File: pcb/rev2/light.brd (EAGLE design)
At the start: 13 x 13 mm, 5 parts, among them J3 FFC3B07-05-T, U1 TEMT6000

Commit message: working on improvments
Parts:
- removed JP1: (no value), adafruit_changed:1X03-CLEANBIG
- added U$1: LS_VERT, apricot:LS_VERT
- moved C1 6.87 mm to (2.79, 5.84), turned to 0 degrees
- moved J3 6.37 mm to (7.85, 11.6), turned to 180 degrees
- moved U1 4.33 mm to (7.85, 4.34), turned to 180 degrees
- moved R5 4.16 mm to (13.1, 5.84), turned to 180 degrees
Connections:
- net +3V3: now also U$1.B1, U$1.B2; no longer JP1.1
- net GND: now also U$1.T1, U$1.T2; no longer JP1.2
- net S: now also U$1.B3, U$1.B4, U$1.T3, U$1.T4; no longer JP1.3
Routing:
- net GND: track 0.00 -> 6.50 mm
- net S: track 9.12 -> 13.7 mm, vias 0 -> 1
- net +3V3: track 17.1 -> 21.2 mm, vias 0 -> 1
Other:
- board size 13 x 13 mm -> 15.7 x 15.6 mm
- board text added: "PulseHPT.com"
- board text removed: "G"
- board text removed: "PulseHPT.com dekuNukem 2023"
- board text removed: "S"
- board text removed: "V"

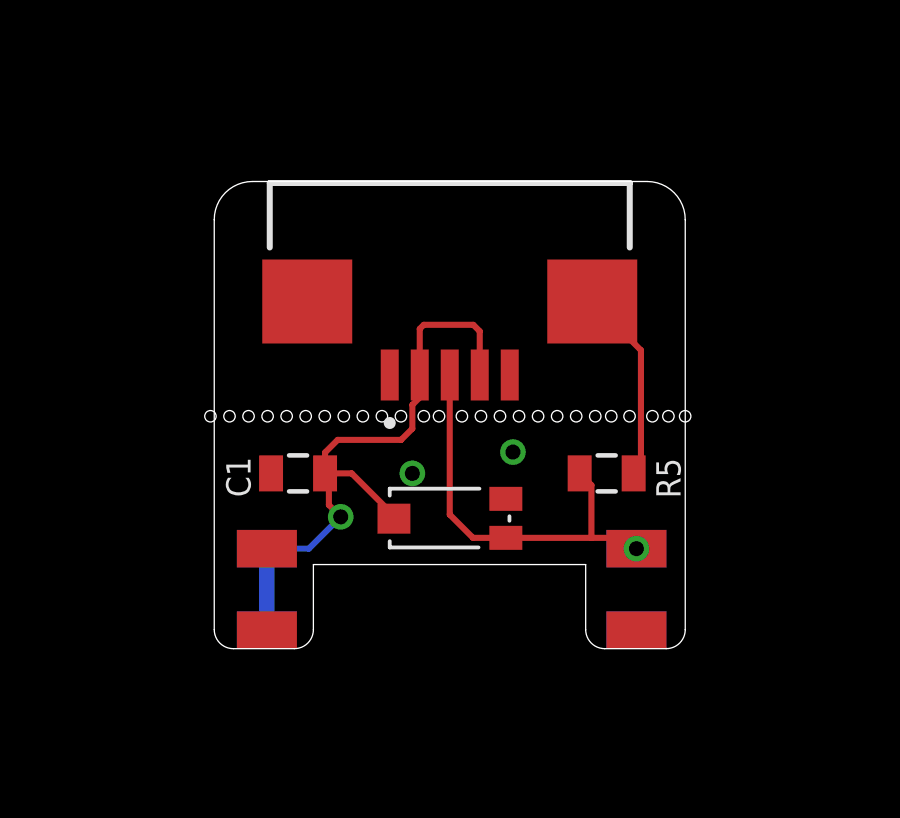
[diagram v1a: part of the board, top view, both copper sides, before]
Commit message: adjusted for pcb thickness
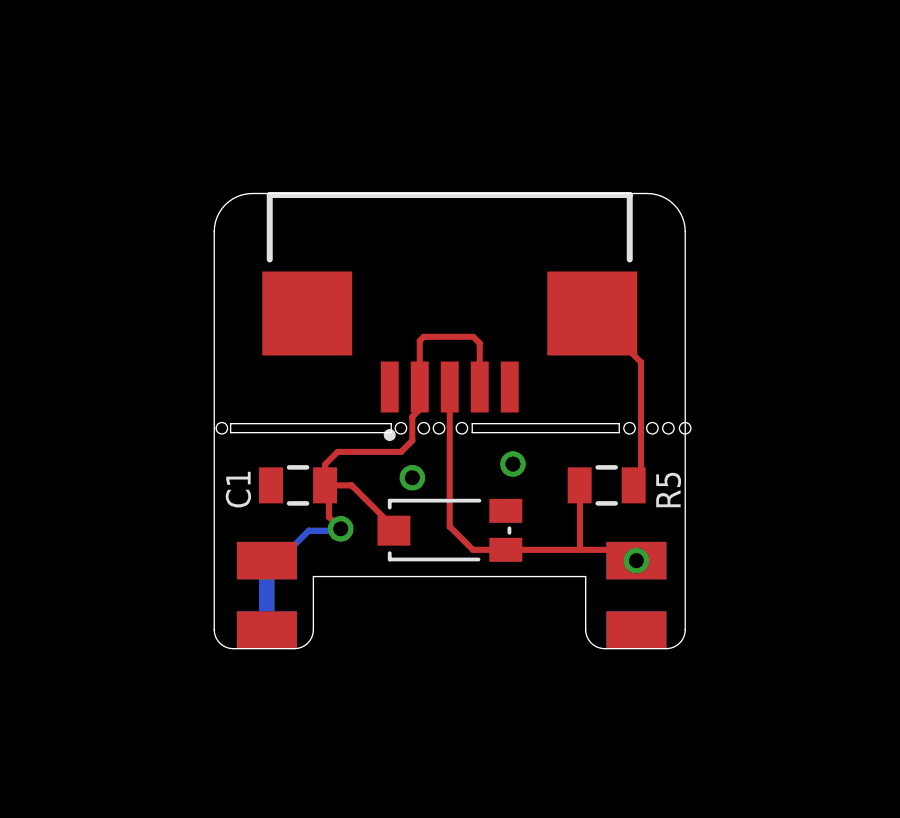
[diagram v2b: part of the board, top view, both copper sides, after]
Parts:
- moved U1 0.40 mm to (7.85, 3.94)
- moved C1 0.40 mm to (2.79, 5.44)
- moved R5 0.40 mm to (13.1, 5.44)
- moved J3 0.40 mm to (7.85, 11.2)
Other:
- board size 15.7 x 15.6 mm -> 15.7 x 15.2 mm

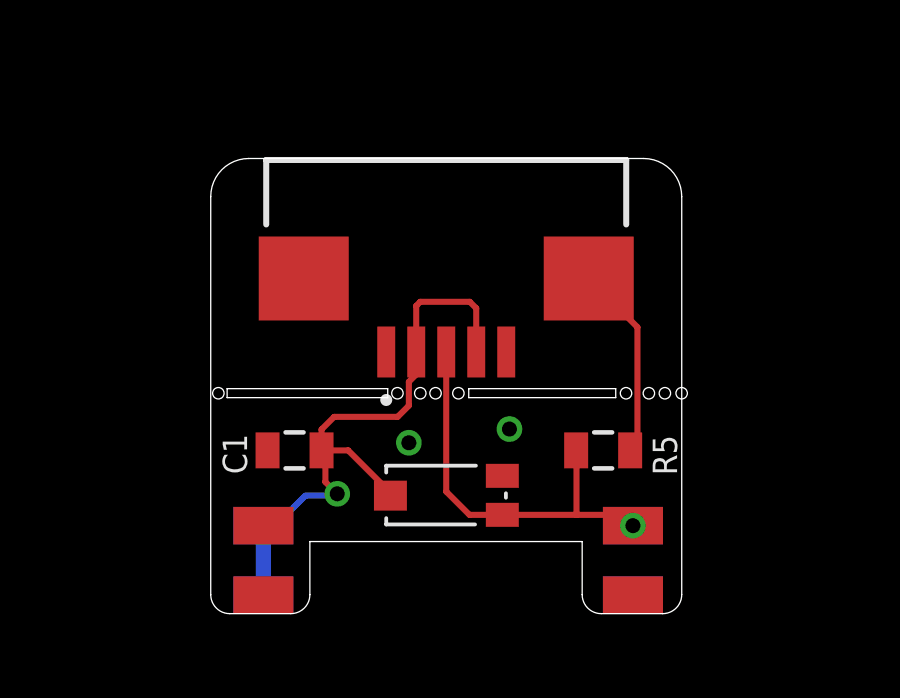
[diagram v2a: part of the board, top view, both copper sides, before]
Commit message: adjusted for pcb thickness
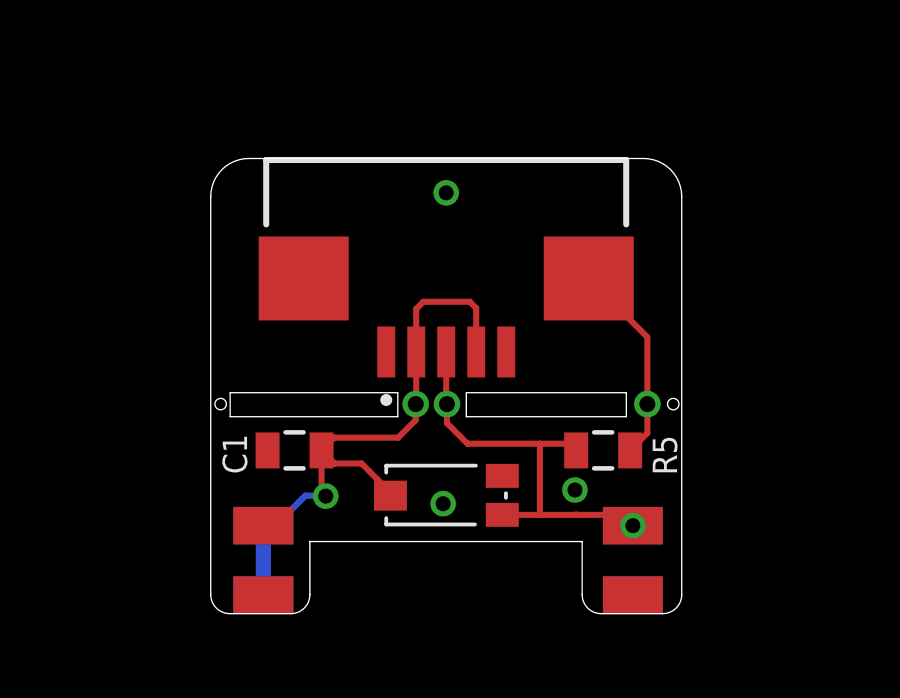
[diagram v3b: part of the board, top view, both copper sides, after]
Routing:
- net +3V3: track 20.8 -> 20.3 mm, vias 1 -> 2
- net S: track 13.7 -> 14.2 mm, vias 1 -> 2
- net GND: track 6.50 -> 6.78 mm, vias 2 -> 4
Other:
- outline, holes or cut-outs redrawn
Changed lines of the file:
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@@
 <setting verticaltext="up"/>
 </settings>
-<grid distance="5" unitdist="mil" unit="mil" style="lines" multiple="1" display="no" altdistance="1" altunitdist="mil" altunit="mil"/>
+<grid distance="1" unitdist="mil" unit="mil" style="lines" multiple="1" display="no" altdistance="5" altunitdist="mil" altunit="mil"/>
 <layers>
 <layer number="1" name="Top" color="4" fill="1" visible="yes" active="yes"/>
@@
 <layer number="43" name="vRestrict" color="2" fill="10" visible="no" active="yes"/>
 <layer number="44" name="Drills" color="7" fill="1" visible="no" active="yes"/>
-<layer number="45" name="Holes" color="7" fill="1" visible="yes" active="yes"/>
+<layer number="45" name="Holes" color="7" fill="1" visible="no" active="yes"/>
 <layer number="46" name="Milling" color="3" fill="1" visible="yes" active="yes"/>
 <layer number="47" name="Measures" color="7" fill="1" visible="no" active="yes"/>
@@
 <wire x1="12.381" y1="2.4034" x2="12.381" y2="0.635" width="0" layer="20"/>
 <wire x1="12.381" y1="0.635" x2="13.016" y2="0" width="0" layer="20" curve="90"/>
-<hole x="0.254" y="7.347" drill="0.381"/>
-<hole x="6.223" y="7.347" drill="0.381"/>
-<hole x="7.493" y="7.347" drill="0.381"/>
-<hole x="8.255" y="7.347" drill="0.381"/>
-<hole x="14.605" y="7.347" drill="0.381"/>
-<hole x="15.1384" y="7.347" drill="0.381"/>
-<hole x="6.985" y="7.347" drill="0.381"/>
-<hole x="13.843" y="7.347" drill="0.381"/>
-<hole x="15.6972" y="7.347" drill="0.381"/>
+<hole x="15.4178" y="6.985" drill="0.381"/>
 <polygon width="0" layer="46">
-<vertex x="0.546" y="7.5"/>
-<vertex x="5.9" y="7.5"/>
-<vertex x="5.9" y="7.2"/>
-<vertex x="0.546" y="7.2"/>
+<vertex x="0.6476" y="7.365"/>
+<vertex x="0.6476" y="6.565"/>
+<vertex x="6.235" y="6.565"/>
+<vertex x="6.235" y="7.365"/>
 </polygon>
 <polygon width="0" layer="46">
-<vertex x="8.6" y="7.5"/>
-<vertex x="13.5" y="7.5"/>
-<vertex x="13.5" y="7.2"/>
-<vertex x="8.6" y="7.2"/>
+<vertex x="8.5206" y="7.365"/>
+<vertex x="8.5206" y="6.565"/>
+<vertex x="13.854" y="6.565"/>
+<vertex x="13.854" y="7.365"/>
 </polygon>
+<hole x="0.3302" y="6.985" drill="0.381"/>
 </plain>
 <attributes>
@@
 <contactref element="U$1" pad="T1"/>
 <contactref element="U$1" pad="T2"/>
-<wire x1="12.6" y1="11.172" x2="14.224" y2="9.548" width="0.2032" layer="1"/>
-<via x="6.604" y="5.696" extent="1-16" drill="0.5"/>
-<via x="9.9568" y="6.1532" extent="1-16" drill="0.5"/>
-<wire x1="14.224" y1="9.548" x2="14.224" y2="5.685" width="0.2032" layer="1"/>
-<wire x1="14.224" y1="5.685" x2="13.981" y2="5.442" width="0.2032" layer="1"/>
+<via x="7.747" y="3.664" extent="1-16" drill="0.5"/>
+<via x="12.1412" y="4.1212" extent="1-16" drill="0.5"/>
+<wire x1="14.5542" y1="9.2178" x2="14.5542" y2="6.985" width="0.2032" layer="1"/>
+<via x="14.5542" y="6.985" extent="1-16" drill="0.5334"/>
+<wire x1="12.6" y1="11.172" x2="14.5542" y2="9.2178" width="0.2032" layer="1"/>
+<wire x1="13.981" y1="5.442" x2="14.5542" y2="6.0152" width="0.2032" layer="1"/>
+<wire x1="14.5542" y1="6.0152" x2="14.5542" y2="6.985" width="0.2032" layer="1"/>
+<via x="7.8486" y="14.0272" extent="1-16" drill="0.5"/>
 </signal>
 <signal name="S">
@@
 <contactref element="U$1" pad="T4"/>
 <via x="14.073" y="2.933" extent="1-16" drill="0.5"/>
-<wire x1="8.626" y1="3.293" x2="9.72" y2="3.293" width="0.2032" layer="1"/>
-<wire x1="7.85" y1="8.722" x2="7.85" y2="4.069" width="0.2032" layer="1"/>
-<wire x1="7.85" y1="4.069" x2="8.626" y2="3.293" width="0.2032" layer="1"/>
-<wire x1="9.72" y1="3.293" x2="12.192" y2="3.293" width="0.2032" layer="1"/>
+<wire x1="9.72" y1="3.293" x2="10.9728" y2="3.293" width="0.2032" layer="1"/>
+<wire x1="10.9728" y1="3.293" x2="12.192" y2="3.293" width="0.2032" layer="1"/>
 <wire x1="12.192" y1="3.293" x2="14.073" y2="3.293" width="0.2032" layer="1"/>
 <wire x1="12.181" y1="5.442" x2="12.192" y2="5.431" width="0.2032" layer="1"/>
-<wire x1="12.192" y1="5.431" x2="12.192" y2="3.293" width="0.2032" layer="1"/>
 <wire x1="14.073" y1="3.293" x2="14.073" y2="2.933" width="0.2032" layer="1"/>
+<wire x1="7.85" y1="8.722" x2="7.85" y2="7.009" width="0.2032" layer="1"/>
+<wire x1="7.85" y1="7.009" x2="7.874" y2="6.985" width="0.2032" layer="1"/>
+<via x="7.874" y="6.985" extent="1-16" drill="0.5334"/>
+<wire x1="7.874" y1="6.985" x2="7.874" y2="6.35" width="0.2032" layer="1"/>
+<wire x1="7.874" y1="6.35" x2="8.5598" y2="5.6642" width="0.2032" layer="1"/>
+<wire x1="11.9588" y1="5.6642" x2="12.181" y2="5.442" width="0.2032" layer="1"/>
+<wire x1="8.5598" y1="5.6642" x2="10.9728" y2="5.6642" width="0.2032" layer="1"/>
+<wire x1="10.9728" y1="5.6642" x2="11.9588" y2="5.6642" width="0.2032" layer="1"/>
+<wire x1="12.181" y1="3.304" x2="12.192" y2="3.293" width="0.2032" layer="1"/>
+<wire x1="10.9728" y1="5.6642" x2="10.9728" y2="3.293" width="0.2032" layer="1"/>
 <wire x1="14.073" y1="0.6168" x2="14.073" y2="0.6168" width="0" layer="19" extent="1-16"/>
 <wire x1="14.073" y1="2.933" x2="14.073" y2="0.6168" width="0" layer="19" extent="16-16"/>
@@
 <contactref element="U$1" pad="B1"/>
 <contactref element="U$1" pad="B2"/>
-<wire x1="6.85" y1="8.722" x2="6.85" y2="10.26" width="0.2032" layer="1"/>
-<wire x1="6.85" y1="10.26" x2="6.985" y2="10.395" width="0.2032" layer="1"/>
-<wire x1="6.985" y1="10.395" x2="8.636" y2="10.395" width="0.2032" layer="1"/>
+<wire x1="6.85" y1="8.722" x2="6.85" y2="10.1584" width="0.2032" layer="1"/>
+<wire x1="6.85" y1="10.1584" x2="7.0866" y2="10.395" width="0.2032" layer="1"/>
+<wire x1="7.0866" y1="10.395" x2="8.636" y2="10.395" width="0.2032" layer="1"/>
 <wire x1="8.636" y1="10.395" x2="8.85" y2="10.181" width="0.2032" layer="1"/>
 <wire x1="8.85" y1="10.181" x2="8.85" y2="8.722" width="0.2032" layer="1"/>
-<wire x1="6.85" y1="8.722" x2="6.85" y2="7.974" width="0.2032" layer="1"/>
-<wire x1="6.85" y1="7.974" x2="6.604" y2="7.728" width="0.2032" layer="1"/>
-<wire x1="6.604" y1="7.728" x2="6.604" y2="6.9346" width="0.2032" layer="1"/>
-<wire x1="3.821" y1="4.3896" x2="4.2164" y2="3.9942" width="0.2032" layer="1"/>
-<via x="4.2164" y="3.9942" extent="1-16" drill="0.5"/>
-<wire x1="6.604" y1="6.9346" x2="6.229" y2="6.5596" width="0.2032" layer="1"/>
-<wire x1="3.694" y1="6.1388" x2="3.694" y2="5.442" width="0.2032" layer="1"/>
-<wire x1="6.229" y1="6.5596" x2="4.1148" y2="6.5596" width="0.2032" layer="1"/>
-<wire x1="4.1148" y1="6.5596" x2="3.694" y2="6.1388" width="0.2032" layer="1"/>
-<wire x1="3.694" y1="5.442" x2="3.821" y2="5.315" width="0.2032" layer="1"/>
-<wire x1="3.821" y1="5.315" x2="3.821" y2="4.3896" width="0.2032" layer="1"/>
-<wire x1="5.99" y1="4.035" x2="4.583" y2="5.442" width="0.2032" layer="1"/>
-<wire x1="3.694" y1="5.442" x2="4.583" y2="5.442" width="0.2032" layer="1"/>
-<wire x1="5.99" y1="3.933" x2="5.99" y2="4.035" width="0.2032" layer="1"/>
+<via x="3.8354" y="3.918" extent="1-16" drill="0.5"/>
 <wire x1="1.754" y1="2.933" x2="1.754" y2="0.6168" width="0.508" layer="16"/>
-<wire x1="4.2164" y1="3.9942" x2="4.1552" y2="3.933" width="0.2032" layer="16"/>
-<wire x1="4.1552" y1="3.933" x2="3.154" y2="3.933" width="0.2032" layer="16"/>
+<wire x1="3.8354" y1="3.918" x2="3.8204" y2="3.933" width="0.2032" layer="16"/>
+<wire x1="3.8204" y1="3.933" x2="3.154" y2="3.933" width="0.2032" layer="16"/>
 <wire x1="3.154" y1="3.933" x2="2.154" y2="2.933" width="0.2032" layer="16"/>
 <wire x1="2.154" y1="2.933" x2="1.754" y2="2.933" width="0.2032" layer="16"/>
+<wire x1="6.85" y1="8.722" x2="6.85" y2="7.0024" width="0.2032" layer="1"/>
+<wire x1="6.85" y1="7.0024" x2="6.8326" y2="6.985" width="0.2032" layer="1"/>
+<via x="6.8326" y="6.985" extent="1-16" drill="0.5334"/>
+<wire x1="6.8326" y1="6.985" x2="6.8326" y2="6.4516" width="0.2032" layer="1"/>
+<wire x1="4.1194" y1="5.8674" x2="3.694" y2="5.442" width="0.2032" layer="1"/>
+<wire x1="6.8326" y1="6.4516" x2="6.2484" y2="5.8674" width="0.2032" layer="1"/>
+<wire x1="6.2484" y1="5.8674" x2="4.1194" y2="5.8674" width="0.2032" layer="1"/>
+<wire x1="3.8354" y1="3.918" x2="3.694" y2="4.0594" width="0.2032" layer="1"/>
+<wire x1="3.694" y1="4.0594" x2="3.694" y2="5.442" width="0.2032" layer="1"/>
+<wire x1="3.694" y1="5.442" x2="4.1322" y2="5.0038" width="0.2032" layer="1"/>
+<wire x1="4.1322" y1="5.0038" x2="5.0292" y2="5.0038" width="0.2032" layer="1"/>
+<wire x1="5.0292" y1="5.0038" x2="5.99" y2="4.043" width="0.2032" layer="1"/>
+<wire x1="5.99" y1="4.043" x2="5.99" y2="3.933" width="0.2032" layer="1"/>
 </signal>
 </signals>
